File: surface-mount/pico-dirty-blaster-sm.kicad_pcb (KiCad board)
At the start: 2 copper layers, 15.2 x 15.2 mm, 3 parts, among them J1 Conn_01x06, J2 Conn_02x05_Counter_Clockwise, J3 Conn_02x05_Counter_Clockwise

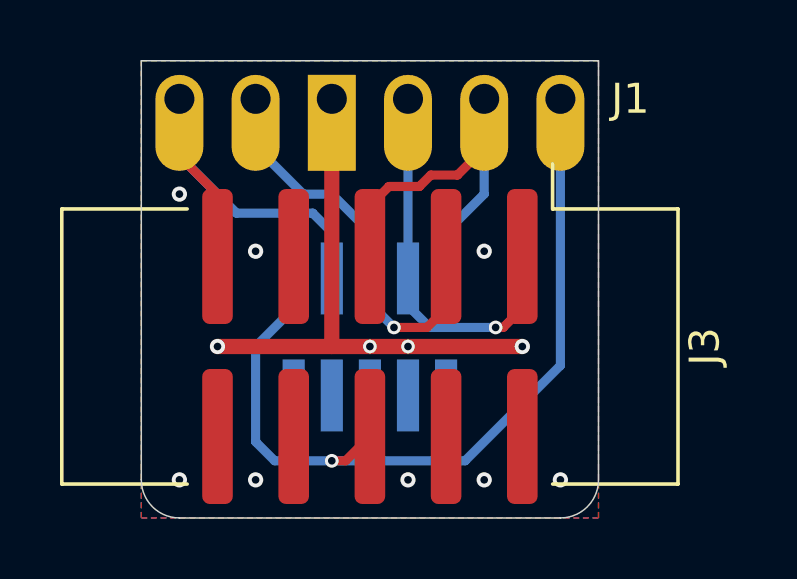
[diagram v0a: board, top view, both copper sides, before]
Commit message: connected vcc on SM, 0402 R on LS
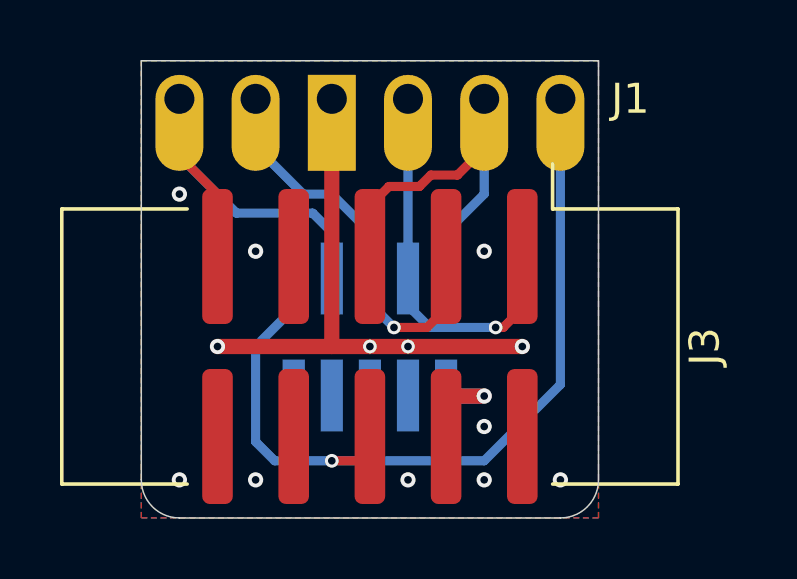
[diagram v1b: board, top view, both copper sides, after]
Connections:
- J2 pad 1: unconnected-(J2-Pin_1-Pad1) -> /J_VCC
- J3 pad 4: unconnected-(J3-Pin_4-Pad4) -> /J_VCC
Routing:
- net /J_VCC: track 0.00 -> 3.82 mm, vias 0 -> 1
- net /J_RST: track 28.2 -> 29.0 mm
- net /J_GND: vias 12 -> 13
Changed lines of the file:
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@@
   (net 5 "/J_TDO")
   (net 6 "/J_TDI")
-  (net 7 "unconnected-(J2-Pin_1-Pad1)")
+  (net 7 "/J_VCC")
   (net 8 "unconnected-(J2-Pin_7-Pad7)")
   (net 9 "unconnected-(J2-Pin_9-Pad9)")
-  (net 10 "unconnected-(J3-Pin_4-Pad4)")
-  (net 11 "unconnected-(J3-Pin_7-Pad7)")
-  (net 12 "unconnected-(J3-Pin_8-Pad8)")
+  (net 10 "unconnected-(J3-Pin_7-Pad7)")
+  (net 11 "unconnected-(J3-Pin_8-Pad8)")
   (footprint "custom:BHR-10-VSG-SMT_2x05_P2.54mm_Vertical_SMD" (layer "F.Cu")
     (at 152.4 101.6 -90)
     (descr "SMD IDC box header, 2x05, 2.54mm pitch, DIN 41651 / IEC 60603-13, double rows, https://www.tme.eu/Document/4baa0e952ce73e37bc68cf730b541507/T821M114A1S100CEU-B.pdf")
     (tags "SMD vertical IDC box header  2x05 2.54mm double row")
-    (property "Sheetfile" "pico-dirty-blasterd-sm.kicad_sch")
+    (property "Sheetfile" "pico-dirty-blaster-sm.kicad_sch")
     (property "Sheetname" "")
     (property "ki_description" "Generic connector, double row, 02x05, odd/even pin numbering scheme (row 1 odd numbers, row 2 even numbers), script generated (kicad-library-utils/schlib/autogen/connector/)")
@@
       (net 5 "/J_TDO") (pinfunction "Pin_3") (pintype "passive"))
     (pad "4" smd roundrect (at 3 -2.54 270) (size 4.5 1.02) (layers "F.Cu" "F.Paste" "F.Mask") (roundrect_rratio 0.25)
-      (net 10 "unconnected-(J3-Pin_4-Pad4)") (pinfunction "Pin_4") (pintype "passive"))
+      (net 7 "/J_VCC") (pinfunction "Pin_4") (pintype "passive"))
     (pad "5" smd roundrect (at -3 0 270) (size 4.5 1.02) (layers "F.Cu" "F.Paste" "F.Mask") (roundrect_rratio 0.25)
       (net 2 "/J_TMS") (pinfunction "Pin_5") (pintype "passive"))
@@
       (net 1 "/J_RST") (pinfunction "Pin_6") (pintype "passive"))
     (pad "7" smd roundrect (at -3 2.54 270) (size 4.5 1.02) (layers "F.Cu" "F.Paste" "F.Mask") (roundrect_rratio 0.25)
-      (net 11 "unconnected-(J3-Pin_7-Pad7)") (pinfunction "Pin_7") (pintype "passive"))
+      (net 10 "unconnected-(J3-Pin_7-Pad7)") (pinfunction "Pin_7") (pintype "passive"))
     (pad "8" smd roundrect (at 3 2.54 270) (size 4.5 1.02) (layers "F.Cu" "F.Paste" "F.Mask") (roundrect_rratio 0.25)
-      (net 12 "unconnected-(J3-Pin_8-Pad8)") (pinfunction "Pin_8") (pintype "passive"))
+      (net 11 "unconnected-(J3-Pin_8-Pad8)") (pinfunction "Pin_8") (pintype "passive"))
     (pad "9" smd roundrect (at -3 5.08 270) (size 4.5 1.02) (layers "F.Cu" "F.Paste" "F.Mask") (roundrect_rratio 0.25)
       (net 6 "/J_TDI") (pinfunction "Pin_9") (pintype "passive"))
@@
     (descr "Through hole straight pin header, 1x06, 2.54mm pitch, single row")
     (tags "Through hole pin header THT 1x06 2.54mm single row")
-    (property "Sheetfile" "pico-dirty-blasterd-sm.kicad_sch")
+    (property "Sheetfile" "pico-dirty-blaster-sm.kicad_sch")
     (property "Sheetname" "")
     (property "ki_description" "Generic connector, single row, 01x06, script generated (kicad-library-utils/schlib/autogen/connector/)")
@@
     (descr "surface-mounted straight pin header, 2x05, 1.27mm pitch, double rows")
     (tags "Surface mounted pin header SMD 2x05 1.27mm double row")
-    (property "Sheetfile" "pico-dirty-blasterd-sm.kicad_sch")
+    (property "Sheetfile" "pico-dirty-blaster-sm.kicad_sch")
     (property "Sheetname" "")
     (property "ki_description" "Generic connector, double row, 02x05, odd/even pin numbering scheme (row 1 odd numbers, row 2 even numbers), script generated (kicad-library-utils/schlib/autogen/connector/)")
@@
       (stroke (width 0.1) (type solid)) (layer "B.Fab"))
     (pad "1" smd rect (at -1.95 2.54 90) (size 2.4 0.74) (layers "B.Cu" "B.Paste" "B.Mask")
-      (net 7 "unconnected-(J2-Pin_1-Pad1)") (pinfunction "Pin_1") (pintype "passive"))
+      (net 7 "/J_VCC") (pinfunction "Pin_1") (pintype "passive"))
     (pad "2" smd rect (at 1.95 2.54 90) (size 2.4 0.74) (layers "B.Cu" "B.Paste" "B.Mask")
       (net 2 "/J_TMS") (pinfunction "Pin_2") (pintype "passive"))
@@
     (effects (font (size 1.016 0.889) (thickness 0.127)) (justify left mirror))
   )
-  (segment (start 151.59 105.41) (end 152.4 104.6) (width 0.3048) (layer "F.Cu") (net 1))
-  (segment (start 151.13 105.41) (end 151.59 105.41) (width 0.3048) (layer "F.Cu") (net 1))
+  (segment (start 152.4 104.6) (end 152.4 105.41) (width 0.3048) (layer "F.Cu") (net 1))
+  (segment (start 152.4 105.41) (end 151.13 105.41) (width 0.3048) (layer "F.Cu") (net 1))
   (via (at 151.13 105.41) (size 0.457) (drill 0.254) (layers "F.Cu" "B.Cu") (net 1))
   (segment (start 149.86 99.3325) (end 149.86 100.33) (width 0.3048) (layer "B.Cu") (net 1))
-  (segment (start 158.75 93.345) (end 158.75 102.235) (width 0.3048) (layer "B.Cu") (net 1))
   (segment (start 148.59 101.6) (end 148.59 104.775) (width 0.3048) (layer "B.Cu") (net 1))
   (segment (start 148.59 104.775) (end 149.225 105.41) (width 0.3048) (layer "B.Cu") (net 1))
+  (segment (start 158.75 102.87) (end 156.21 105.41) (width 0.3048) (layer "B.Cu") (net 1))
   (segment (start 149.86 100.33) (end 148.59 101.6) (width 0.3048) (layer "B.Cu") (net 1))
-  (segment (start 155.575 105.41) (end 151.13 105.41) (width 0.3048) (layer "B.Cu") (net 1))
+  (segment (start 158.75 93.345) (end 158.75 102.87) (width 0.3048) (layer "B.Cu") (net 1))
+  (segment (start 156.21 105.41) (end 151.13 105.41) (width 0.3048) (layer "B.Cu") (net 1))
   (segment (start 149.225 105.41) (end 151.13 105.41) (width 0.3048) (layer "B.Cu") (net 1))
-  (segment (start 158.75 102.235) (end 155.575 105.41) (width 0.3048) (layer "B.Cu") (net 1))
   (segment (start 153.035 96.266) (end 154.051 96.266) (width 0.3048) (layer "F.Cu") (net 2))
   (segment (start 156.21 94.996) (end 156.21 93.345) (width 0.3048) (layer "F.Cu") (net 2))
@@
   (via (at 157.48 101.6) (size 0.508) (drill 0.254) (layers "F.Cu" "B.Cu") (net 4))
   (via (at 156.21 106.045) (size 0.508) (drill 0.254) (layers "F.Cu" "B.Cu") (net 4))
+  (via (at 156.21 104.267) (size 0.508) (drill 0.254) (layers "F.Cu" "B.Cu") (net 4))
   (via (at 148.59 106.045) (size 0.508) (drill 0.254) (layers "F.Cu" "B.Cu") (net 4))
   (via (at 153.67 101.6) (size 0.457) (drill 0.254) (layers "F.Cu" "B.Cu") (net 4))
@@
   (segment (start 146.05 95.25) (end 146.05 93.345) (width 0.3048) (layer "B.Cu") (net 6))
   (segment (start 150.495 97.155) (end 147.955 97.155) (width 0.3048) (layer "B.Cu") (net 6))
+  (segment (start 155.067 103.251) (end 154.94 103.378) (width 0.3048) (layer "F.Cu") (net 7))
+  (segment (start 154.94 103.378) (end 154.94 104.6) (width 0.3048) (layer "F.Cu") (net 7))
+  (segment (start 156.21 103.251) (end 155.067 103.251) (width 0.508) (layer "F.Cu") (net 7))
+  (via (at 156.21 103.251) (size 0.508) (drill 0.254) (layers "F.Cu" "B.Cu") (net 7))
+  (segment (start 154.9585 103.251) (end 154.94 103.2325) (width 0.3048) (layer "B.Cu") (net 7))
+  (segment (start 156.21 103.251) (end 154.9585 103.251) (width 0.508) (layer "B.Cu") (net 7))
   (zone (net 4) (net_name "/J_GND") (layers "F&B.Cu") (hatch edge 0.5)
     (connect_pads (clearance 0.254))
